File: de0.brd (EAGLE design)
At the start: 160 x 100 mm, 69 parts, among them IC1 PL2303SA__LF, J2 UX60SC-MB-5ST, U1 P0082, U2 RFM95W-915S2, U3 TPS76201DBVR, U4 TPS76201DBVR, U5 TPS76201DBVR

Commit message: Add files via upload
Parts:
- removed JP10: VDD, jumper:JP1
- removed JP8: VBP, jumper:JP1
- removed JP9: VBN, jumper:JP1
- added ADDRESS_0, ADDRESS_1, ADDRESS_10, ADDRESS_11, ADDRESS_12, ADDRESS_13, ADDRESS_14, ADDRESS_15, ADDRESS_2, ADDRESS_3, ADDRESS_4, ADDRESS_5, ADDRESS_6, ADDRESS_7, ADDRESS_8, ADDRESS_9, CLOCK, RD_DATA_0, RD_DATA_2, RD_DATA_3, RD_DATA_4, RD_DATA_5, RD_DATA_6, RD_DATA_7, RD_EN, U$4, U$40, U$48, U$49, U$50, U$51, U$52, U$53, USEC_TICK, WR_DATA_0, WR_DATA_1, WR_DATA_2, WR_DATA_3, WR_DATA_4, WR_DATA_5, WR_DATA_7, WR_EN: (no value), qfp160:POINT
- added C11, C13, C15, C20, C21, C22: 10uF, SparkFun-Capacitors:0603
- added C12, C14, C16, C17, C18, C19: 0.1uF, SparkFun-Capacitors:0603
- added J1: JUMPER_IN_50, jumper:04C
- added J3: REG_OUT_33, jumper:04C
- added JP13: REG_IN_07, jumper:JP1
- added JP14: REG_IN_12, jumper:JP1
- added JP15: REG_OUT_07, jumper:JP1
- added JP16: REG_OUT_12, jumper:JP1
- added JP17: VCCQ, jumper:JP1
- added JP18: VDDH, jumper:JP1
- added JP19: VDDLS, jumper:JP1
- added U$10: INTERRUPTS_0, qfp160:POINT
- added U$11: INTERRUPTS_1, qfp160:POINT
- added U$12: INTERRUPTS_2, qfp160:POINT
- added U$13: INTERRUPTS_3, qfp160:POINT
- added U$14, U$15: INTERRUPTS_5, qfp160:POINT
- added U$16: INTERRUPTS_6, qfp160:POINT
- added U$17: INTERRUPTS_7, qfp160:POINT
- JP3: value VDDLS -> VDD; device jumper:JP2Q -> jumper:JP1
- JP5: value LORA -> REG_IN_33; device jumper:JP6Q -> jumper:JP1
- JP6: value VCCQ -> VBP; device jumper:JP8Q -> jumper:JP1
- JP7: value VDDH -> VBN; device jumper:JP2Q -> jumper:JP1
- U$1: value (none) -> SOCKET
- moved JP7 188.2 mm to (73.1, -7.60)
- moved R7 187.2 mm to (-2.90, -15.8), turned to 90 degrees
- moved R6 186.7 mm to (0.10, -15.8), turned to 90 degrees
- moved R5 186.2 mm to (3.10, -15.8), turned to 90 degrees
- moved R4 185.7 mm to (6.10, -15.8), turned to 90 degrees
- moved R3 185.3 mm to (9.10, -15.8), turned to 90 degrees
- moved JP6 185.1 mm to (68.4, -7.40)
- moved R2 184.9 mm to (12.2, -15.8), turned to 90 degrees
- moved R1 184.4 mm to (15.2, -15.8), turned to 90 degrees
- moved JP12 183.6 mm to (74.0, -28.5)
- moved SV2 177.1 mm to (-53.5, -45.5)
- moved S5 174.4 mm to (30.9, -26.0), turned to 270 degrees
- moved D8 174.1 mm to (-5.90, -11.8), turned to 270 degrees
- moved D7 173.7 mm to (-2.90, -11.8), turned to 270 degrees
- moved D6 173.3 mm to (0.10, -11.8), turned to 268.9 degrees
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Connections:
- net GPIO-1_VCC_SYS renamed GPIO1_VCC_5V
- removed net GPIO-0_VCC3P3: U1.JP1_29
- removed net GPIO-0_VCC_SYS: U1.JP1_11
- removed net GPIO-1_VCC3P3: U1.JP2_29
- removed net N$12: JP2.7, U1.JP2_3
- removed net N$23: JP5.2, U2.2
- removed net N$25: JP5.6, U2.5
- removed net N$26: JP5.8, U2.6
- removed net N$28: JP5.12, U2.3
- removed net N$37: JP5.10, U2.14
- removed net VCCQ_0: JP6.2, U$1.49
- removed net VCCQ_1: JP6.4, U$1.62
- removed net VCCQ_2: JP6.6, U$1.83
- removed net VCCQ_3: JP6.8, U$1.93
- removed net VCCQ_4: JP6.10, U$1.105
- removed net VCCQ_5: JP6.12, U$1.114
- removed net VCCQ_6: JP6.14, U$1.135
- removed net VCCQ_7: JP6.16, U$1.145
- removed net VDDH_0: JP7.2, U$1.29
- removed net VDDH_1: JP7.4, U$1.99
- removed net VDDLS_0: JP3.2, U$1.33
- removed net VDDLS_1: JP3.4, U$1.103
- new net GPIO0_VCC_5V: J1.3, U1.JP1_11
- new net IN_07: C9.1, JP13.2, U3.1
- new net IN_12: C6.1, JP14.2, U4.1
- new net IN_33: C3.1, JP5.2, U5.1
- new net OUT_07: C10.1, JP15.1, R12.2, U3.5
- new net OUT_12: C7.1, JP16.1, R18.2, U4.5
- new net OUT_33: C4.1, J3.1, R19.2, U5.5
- new net VCCQ: C11.1, C12.1, JP17.2, U$1.105, U$1.114, U$1.135, U$1.145, U$1.49, U$1.62, U$1.83, U$1.93
- new net VDD5_USB: C2.+, D9.A, J1.1, J2.1
- new net VDDH: C13.1, C14.1, JP18.2, U$1.29, U$1.99
- new net VDDLS: C15.1, C16.1, JP19.2, U$1.103, U$1.33
- new net VO_FPGA_33: J3.3, U1.JP1_29, U1.JP2_29
- net ADDRESS_0: now also ADDRESS_0.1, U1.JP1_20; no longer U1.JP1_2
- net ADDRESS_1: now also ADDRESS_1.1, U1.JP1_22; no longer U1.JP1_4
- net ADDRESS_10: now also ADDRESS_10.1, U1.JP1_33; no longer U1.JP1_15
- net ADDRESS_11: now also ADDRESS_11.1, U1.JP1_35; no longer U1.JP1_16
- net ADDRESS_12: now also ADDRESS_12.1, U1.JP1_37; no longer U1.JP1_17
- net ADDRESS_13: now also ADDRESS_13.1, U1.JP1_39; no longer U1.JP1_18
- net ADDRESS_14: now also ADDRESS_14.1, U1.JP1_31; no longer U1.JP1_19
- net ADDRESS_15: now also ADDRESS_15.1, U1.JP1_27; no longer U1.JP1_21
- net ADDRESS_2: now also ADDRESS_2.1, U1.JP1_24; no longer U1.JP1_5
- net ADDRESS_3: now also ADDRESS_3.1, U1.JP1_26; no longer U1.JP2_31
- net ADDRESS_4: now also ADDRESS_4.1, U1.JP1_28; no longer U1.JP1_7
- net ADDRESS_5: now also ADDRESS_5.1, U1.JP1_32; no longer U1.JP1_8
- net ADDRESS_6: now also ADDRESS_6.1, U1.JP1_34; no longer U1.JP1_9
- net ADDRESS_7: now also ADDRESS_7.1, U1.JP1_36; no longer U1.JP1_10
- net ADDRESS_8: now also ADDRESS_8.1, U1.JP1_38; no longer U1.JP1_13
- net ADDRESS_9: now also ADDRESS_9.1, U1.JP1_40; no longer U1.JP1_14
- net CLOCK: now also CLOCK.1, U1.JP2_9; no longer U1.JP2_32
- net GND: now also C11.2, C12.2, C13.2, C14.2, C15.2, C16.2, C17.2, C18.2, C19.2, C20.2, C21.2, C22.2, JP7.1; no longer JP9.1
- net GPIO_OUT_0: now also U1.JP2_18; no longer U1.JP1_20
- net GPIO_OUT_1: now also U1.JP2_20; no longer U1.JP2_13
- net GPIO_OUT_2: now also U1.JP2_22; no longer U1.JP2_14
- net GPIO_OUT_3: now also U1.JP2_24; no longer U1.JP2_15
- net GPIO_OUT_4: now also U1.JP2_26; no longer U1.JP2_16
- net INTERRUPTS_0: now also U$10.1
- net INTERRUPTS_1: now also U$11.1
- net INTERRUPTS_2: now also U$12.1, U1.JP2_6; no longer U1.JP2_5
- net INTERRUPTS_3: now also U$13.1, U1.JP2_8; no longer U1.JP2_6
- net INTERRUPTS_4: now also U$14.1, U1.JP2_10; no longer U1.JP2_7
- net INTERRUPTS_5: now also U$15.1, U1.JP2_14; no longer U1.JP2_8
- net INTERRUPTS_6: now also U$16.1, U1.JP2_16; no longer U1.JP2_9
- net INTERRUPTS_7: now also U$17.1, U1.JP1_16; no longer U1.JP2_10
- net JTAG_TCK: now also U1.JP1_10; no longer U1.JP2_23
- net JTAG_TDI: now also U1.JP1_6; no longer U1.JP2_26
- net JTAG_TDO: now also U1.JP1_14; no longer U1.JP2_22
- net JTAG_TMS: now also U1.JP1_8; no longer U1.JP2_24
- net LORA_DIO0: now also U$53.1, U1.JP2_40, U2.14; no longer JP5.9, U1.JP2_35
- net LORA_MISO: now also U$48.1, U1.JP2_28, U2.2; no longer JP5.1, U1.JP2_36
- net LORA_MOSI: now also U$49.1, U1.JP2_32, U2.3; no longer JP5.11, U1.JP2_37
- net LORA_NSS: now also U$51.1, U1.JP2_36, U2.5; no longer JP5.5, U1.JP2_39
- net LORA_RESET: now also U$52.1, U1.JP2_38, U2.6; no longer JP5.7, U1.JP2_40
- net LORA_SCK: now also U$50.1, U1.JP2_34, U2.4; no longer JP5.3, U1.JP2_38
- net N$11: now also JP2.7; no longer JP2.5
- net N$24: now also JP2.5, U1.JP2_3; no longer JP5.4, U2.4
- net PIN_OUT_0: now also U1.JP2_25; no longer U1.JP1_6
- net PIN_OUT_2: now also U1.JP2_31; no longer U1.JP2_28
- net RD_DATA_0: now also RD_DATA_0.1, U1.JP2_23; no longer U1.JP1_32
- net RD_DATA_1: now also U$4.1, U1.JP2_21; no longer U1.JP1_33
- net RD_DATA_2: now also RD_DATA_2.1, U1.JP2_19; no longer U1.JP1_34
- net RD_DATA_3: now also RD_DATA_3.1, U1.JP2_17; no longer U1.JP1_35
- net RD_DATA_4: now also RD_DATA_4.1, U1.JP2_15; no longer U1.JP1_36
- net RD_DATA_5: now also RD_DATA_5.1, U1.JP2_13; no longer U1.JP1_37
- net RD_DATA_6: now also RD_DATA_6.1, U1.JP2_7; no longer U1.JP1_38
- net RD_DATA_7: now also RD_DATA_7.1, U1.JP2_5; no longer U1.JP1_39
- net RD_EN: now also RD_EN.1, U1.JP1_5; no longer U1.JP2_25
- net SPI_CS: now also U1.JP2_33; no longer U1.JP2_17
- net SPI_MISO: now also U1.JP2_35; no longer U1.JP2_19
- net SPI_MOSI: now also U1.JP2_37; no longer U1.JP2_20
- net SPI_SCK: now also U1.JP2_39; no longer U1.JP2_21
- net UART_RX: now also U1.JP1_4; no longer U1.JP2_33
- net UART_TX: now also U1.JP1_2; no longer U1.JP2_34
- net USEC_TICK: now also U1.JP1_18, USEC_TICK.1; no longer U1.JP2_18
- net VBN: now also C17.1, C21.1, JP7.2; no longer JP9.2
- net VBP: now also C18.1, C20.1, JP6.2; no longer JP8.2
- net VDD: now also C19.1, C22.1, JP3.2; no longer JP10.2
- net VDD5: now also J1.2, JP13.1, JP14.1, JP5.1; no longer C2.+, C3.1, C6.1, C9.1, D9.A, J2.1, U3.1, U4.1, U5.1
- net VO_07: now also JP15.2, JP19.1; no longer C10.1, JP3.1, JP3.3, R12.2, U3.5
- net VO_12: now also JP16.2, JP18.1, JP3.1, JP6.1; no longer C7.1, JP10.1, JP7.1, JP7.3, JP8.1, R18.2, U4.5
- net VO_33: now also J3.2, JP17.1; no longer C4.1, JP6.1, JP6.11, JP6.13, JP6.15, JP6.3, JP6.5, JP6.7, JP6.9, R19.2, U5.5
- net WR_DATA_0: now also U1.JP1_23, WR_DATA_0.1; no longer U1.JP1_22
- net WR_DATA_1: now also U1.JP1_21, WR_DATA_1.1; no longer U1.JP1_23
- net WR_DATA_2: now also U1.JP1_19, WR_DATA_2.1; no longer U1.JP1_24
- net WR_DATA_3: now also U1.JP1_17, WR_DATA_3.1; no longer U1.JP1_25
- net WR_DATA_4: now also U1.JP1_15, WR_DATA_4.1; no longer U1.JP1_26
- net WR_DATA_5: now also U1.JP1_13, WR_DATA_5.1; no longer U1.JP1_27
- net WR_DATA_6: now also U$40.1, U1.JP1_9; no longer U1.JP1_28
- net WR_DATA_7: now also U1.JP1_7, WR_DATA_7.1; no longer U1.JP1_31
- net WR_EN: now also U1.JP1_25, WR_EN.1; no longer U1.JP1_40
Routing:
- net INTERRUPTS_6: track 0.00 -> 147.6 mm
- net INTERRUPTS_5: track 0.00 -> 144.1 mm
- net INTERRUPTS_4: track 0.00 -> 136.4 mm
- net INTERRUPTS_3: track 0.00 -> 131.5 mm
- net INTERRUPTS_2: track 0.00 -> 126.5 mm
- net INTERRUPTS_1: track 0.00 -> 122.1 mm
- net INTERRUPTS_0: track 0.00 -> 115.2 mm
- net USEC_TICK: track 0.00 -> 108.4 mm
- net INTERRUPTS_7: track 0.00 -> 108.4 mm
- net ADDRESS_0: track 0.00 -> 105.1 mm
- net ADDRESS_1: track 0.00 -> 102.0 mm
- net ADDRESS_2: track 0.00 -> 100.4 mm
- net GND: track 0.00 -> 99.2 mm
- net RD_DATA_4: track 0.00 -> 95.2 mm
- net WR_DATA_7: track 0.00 -> 94.7 mm, vias 0 -> 1
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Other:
- board size 160 x 100 mm -> 148.8 x 90.3 mm

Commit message: Connect source for switches
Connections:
- net VO_33: now also S1.1, S2.1, S3.1, S4.1, S5.1, S6.1
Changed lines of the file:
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@@
 <contactref element="J3" pad="2"/>
 <contactref element="JP17" pad="1"/>
+<contactref element="S5" pad="1"/>
+<contactref element="S6" pad="1"/>
+<contactref element="S4" pad="1"/>
+<contactref element="S3" pad="1"/>
+<contactref element="S2" pad="1"/>
+<contactref element="S1" pad="1"/>
+<wire x1="-3.2" y1="-21.89" x2="-21.45" y2="-29.76" width="0" layer="19" extent="1-1"/>
+<wire x1="3.7" y1="-21.89" x2="-3.2" y2="-21.89" width="0" layer="19" extent="1-1"/>
+<wire x1="10.4" y1="-21.79" x2="3.7" y2="-21.89" width="0" layer="19" extent="1-1"/>
+<wire x1="16.9" y1="-21.79" x2="10.4" y2="-21.79" width="0" layer="19" extent="1-1"/>
+<wire x1="30.85" y1="-22.19" x2="16.9" y2="-21.79" width="0" layer="19" extent="1-1"/>
+<wire x1="38.3" y1="-21.99" x2="30.85" y2="-22.19" width="0" layer="19" extent="1-1"/>
+<wire x1="48.1" y1="-8.57" x2="38.3" y2="-21.99" width="0" layer="19" extent="1-1"/>
+<wire x1="-30.3" y1="3.12" x2="-21.45" y2="-29.76" width="0" layer="19" extent="1-1"/>
+<wire x1="-32.72" y1="3.53" x2="-30.3" y2="3.12" width="0" layer="19" extent="1-1"/>
+<wire x1="-19.695" y1="18.6" x2="-30.3" y2="3.12" width="0" layer="19" extent="1-1"/>
+<wire x1="-46.435" y1="16.768" x2="-32.72" y2="3.53" width="0" layer="19" extent="1-1"/>
+<wire x1="-48.975" y1="22.192" x2="-46.435" y2="16.768" width="0" layer="19" extent="1-1"/>
 </signal>
 <signal name="VO_07">

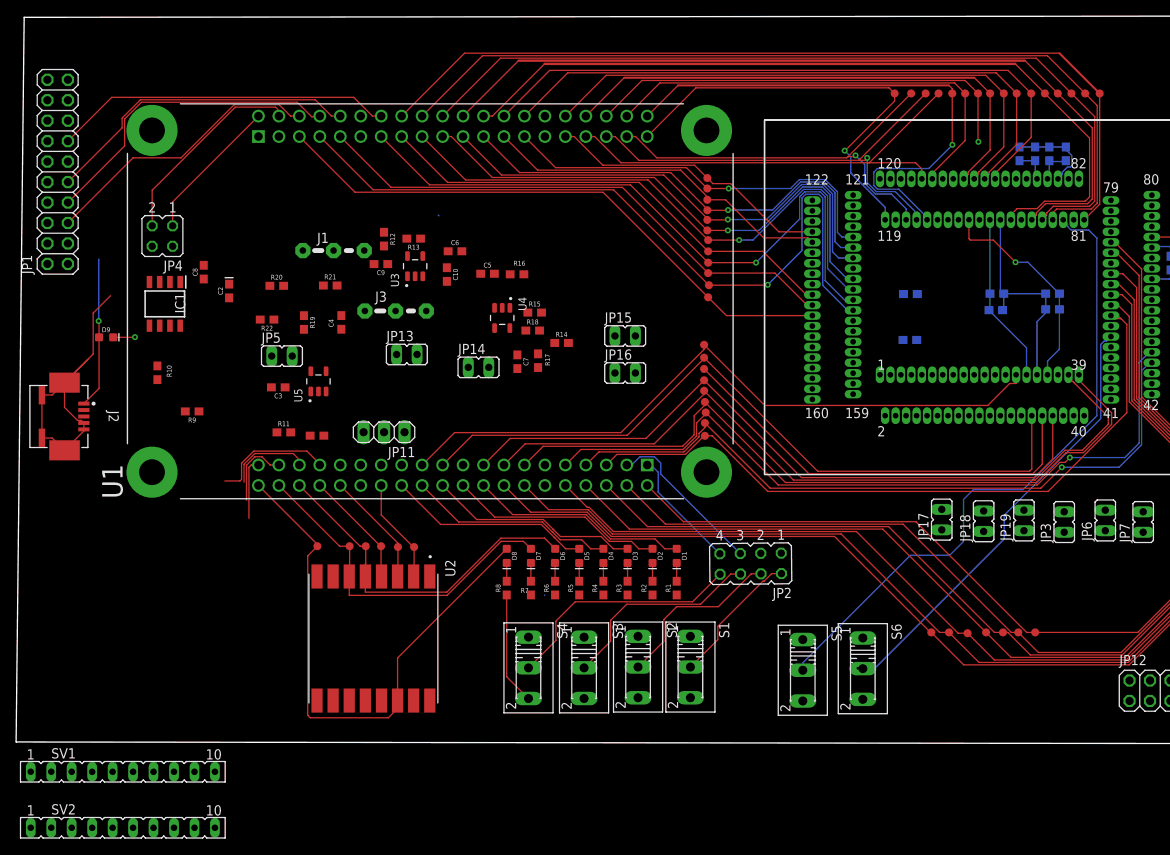
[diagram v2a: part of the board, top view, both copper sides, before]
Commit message: Organize regulator circuits
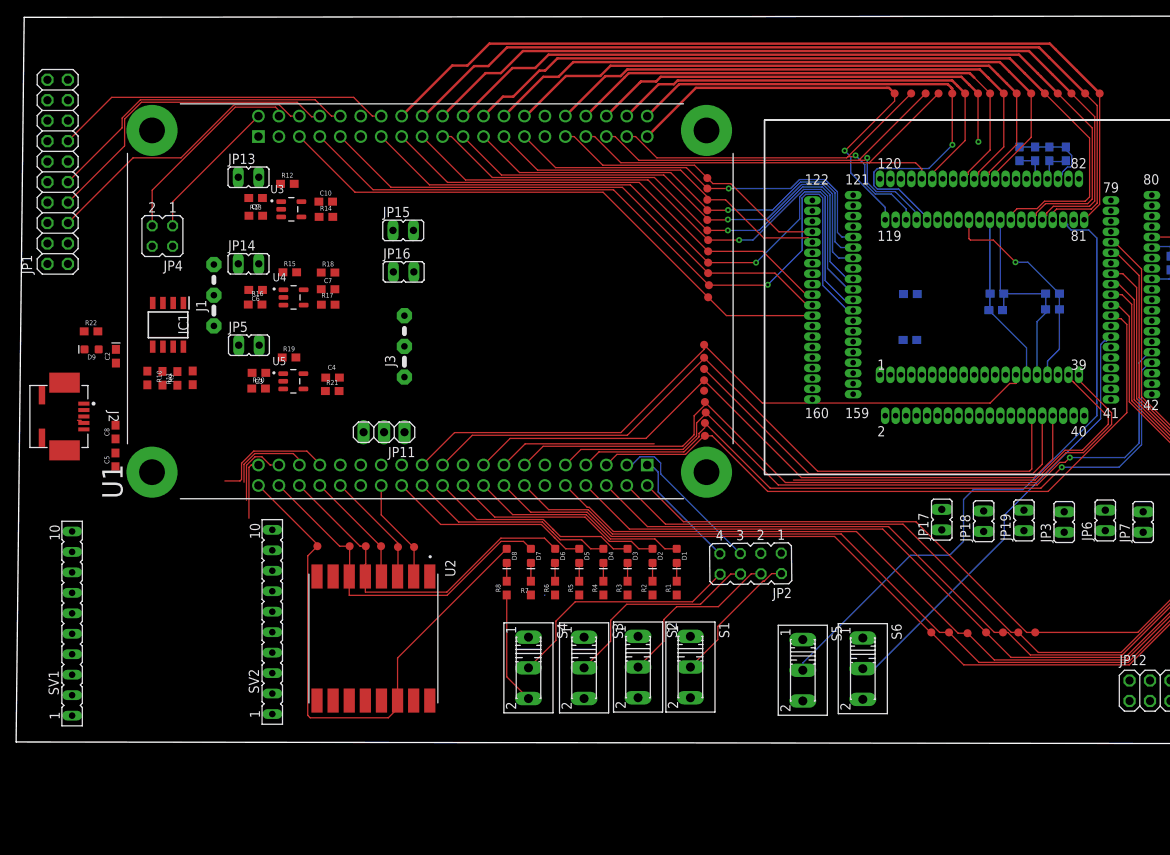
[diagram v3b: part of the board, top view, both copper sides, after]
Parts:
- moved C5 51.6 mm to (-54.5, 0.12), turned to 90 degrees
- moved R14 33.2 mm to (-28.3, 30.3)
- moved R16 32.7 mm to (-37.1, 19.4)
- moved SV2 31.6 mm to (-35.0, -20.0), turned to 90 degrees
- moved JP14 31.3 mm to (-38.0, 24.4)
- moved R15 30.8 mm to (-32.8, 23.4)
- moved JP15 30.5 mm to (-18.8, 28.6)
- moved JP16 30.2 mm to (-18.7, 23.4)
- moved JP13 29.5 mm to (-38.0, 35.2)
- moved R17 27.0 mm to (-28.1, 19.4), turned to 0 degrees
- moved R18 26.4 mm to (-28.1, 23.4)
- moved U4 26.0 mm to (-32.4, 20.3), turned to 0 degrees
- moved C6 25.2 mm to (-37.1, 21.2), turned to 180 degrees
- moved C7 25.2 mm to (-28.1, 21.3), turned to 0 degrees
- moved C8 22.7 mm to (-54.5, 3.57)
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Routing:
- net GND: track 99.2 -> 59.5 mm
- net RD_DATA_4: track 95.2 -> 69.9 mm
- net VDD5_USB: track 18.8 -> 0.00 mm, vias 1 -> 0
- net INTERRUPTS_7: track 108.4 -> 116.5 mm
- net ADDRESS_6: track 64.9 -> 72.1 mm
- net ADDRESS_0: track 105.1 -> 108.2 mm
- net ADDRESS_1: track 102.0 -> 104.8 mm
- net N$36: track 2.74 -> 0.00 mm, vias 1 -> 0
- net LOCKED: track 56.2 -> 53.5 mm, vias 1 -> 0
- net ADDRESS_3: track 81.5 -> 84.0 mm
- net ADDRESS_2: track 100.4 -> 102.6 mm
- net USEC_TICK: track 108.4 -> 109.9 mm
- net ADDRESS_7: track 54.7 -> 55.8 mm
- net ADDRESS_4: track 76.6 -> 77.7 mm
- net ADDRESS_5: track 69.6 -> 70.5 mm
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
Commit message: Update layout
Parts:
- moved JP7 76.5 mm to (5.80, 28.7), turned to 270 degrees
- moved JP6 70.7 mm to (5.90, 25.8), turned to 270 degrees
- moved JP3 64.9 mm to (5.90, 22.8), turned to 270 degrees
- moved JP19 59.0 mm to (5.90, 19.6), turned to 270 degrees
- moved JP18 53.1 mm to (5.90, 16.4), turned to 270 degrees
- moved JP17 47.0 mm to (5.85, 13.3), turned to 270 degrees
- moved U$10 16.2 mm to (47.8, -10.3)
- moved U$11 16.0 mm to (45.9, -10.3)
- moved U$12 16.0 mm to (44.1, -10.3)
- moved U$13 15.7 mm to (42.3, -10.3)
- moved U$14 15.5 mm to (40.5, -10.3)
- moved U$15 15.1 mm to (38.6, -10.3)
- moved U$16 14.8 mm to (36.9, -10.3)
- moved C9 3.93 mm to (-34.2, 29.9), turned to 0 degrees
- moved U3 3.22 mm to (-29.4, 30.9)
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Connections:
- net GND: now also U$1.35, U$1.67
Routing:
- net GND: track 59.5 -> 296.2 mm, vias 0 -> 8
- net VO_33: track 0.00 -> 168.1 mm, vias 0 -> 1
- net VCCQ: track 0.00 -> 140.5 mm, vias 0 -> 4
- net N$10: track 0.00 -> 139.1 mm, vias 0 -> 2
- net N$9: track 0.00 -> 137.9 mm, vias 0 -> 3
- net VDD: track 5.82 -> 87.9 mm, vias 0 -> 2
- net VBP: track 4.43 -> 67.2 mm, vias 0 -> 4
- net VDDH: track 21.2 -> 80.9 mm, vias 0 -> 2
- net VDDLS: track 27.1 -> 86.6 mm, vias 1 -> 3
- net VBN: track 4.29 -> 61.0 mm
- net VO_FPGA_33: track 0.00 -> 53.5 mm
- net VDD5: track 0.00 -> 34.0 mm, vias 0 -> 1
- net SPI_SCK: track 7.63 -> 41.3 mm
- net SPI_MOSI: track 9.23 -> 42.9 mm
- net VO_12: track 0.00 -> 33.2 mm, vias 0 -> 1
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- added copper zone on layer 1, net GND
- added copper zone on layer 16, net V0_12
- added copper zone on layer 16, net VBN
- added copper zone on layer 16, net VBP
- added copper zone on layer 1, net VCCQ
- added copper zone on layer 16, net VCCQ
- added copper zone on layer 1, net VDD
- added copper zone on layer 16, net VDD
- added copper zone on layer 1, net VDDH
- added copper zone on layer 16, net VDDH
- added copper zone on layer 1, net VDDLS
- added copper zone on layer 16, net VDDLS
- added copper zone on layer 1, net VO_07
- added copper zone on layer 1, net VO_12
- added copper zone on layer 16, net VO_33
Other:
- board size 148.8 x 90.3 mm -> 150.7 x 90.7 mm

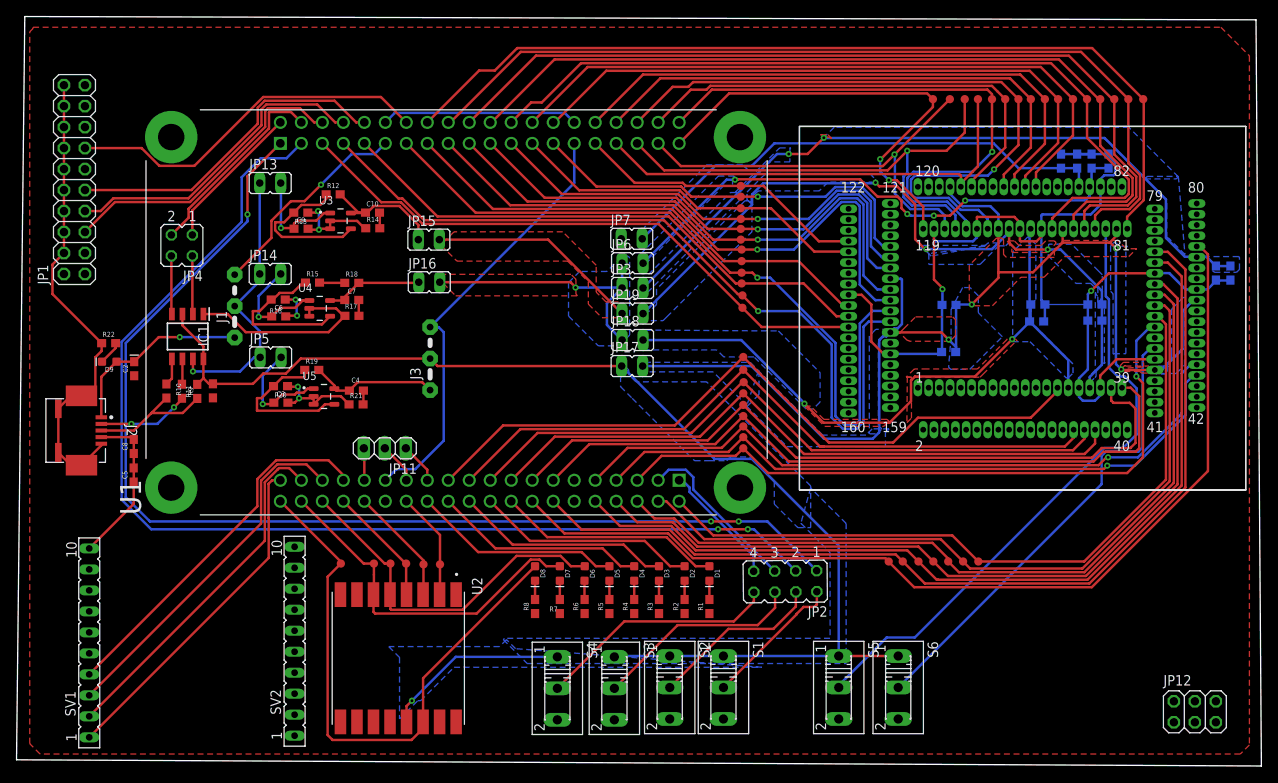
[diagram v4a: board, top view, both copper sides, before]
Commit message: Create plain for power wires
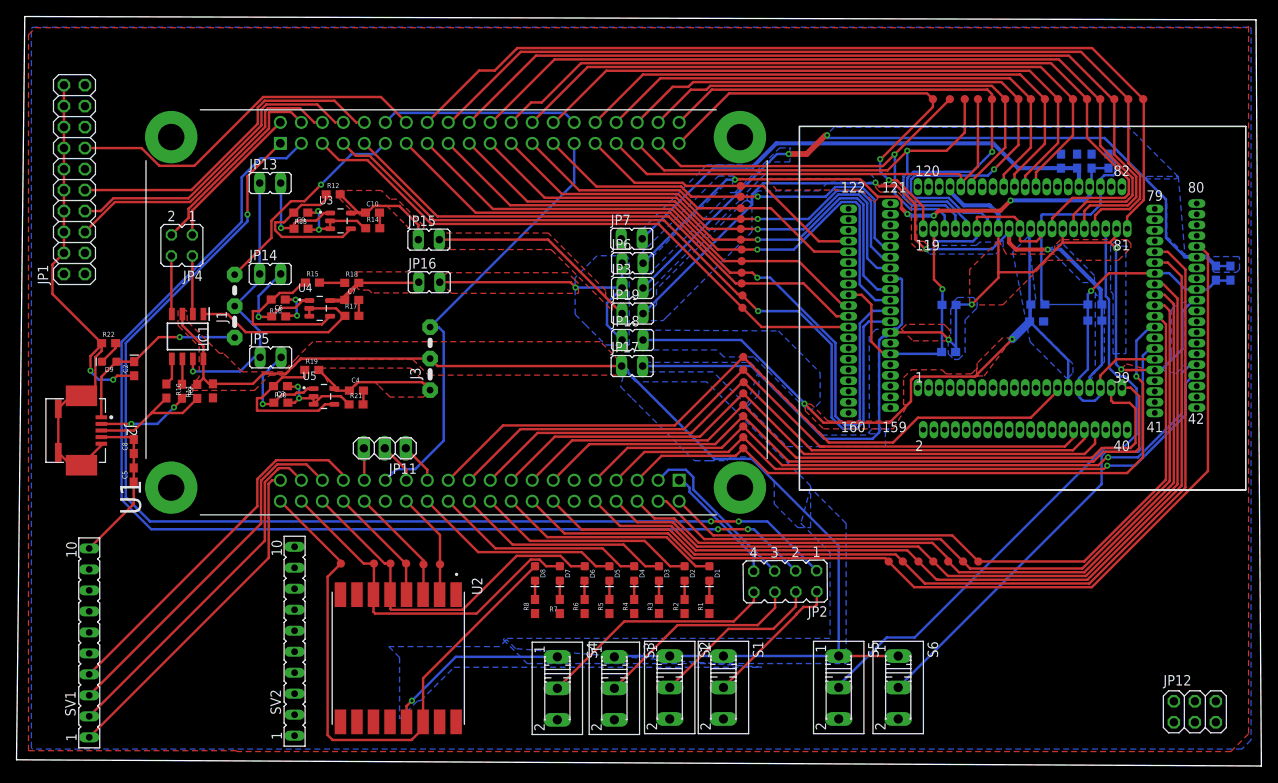
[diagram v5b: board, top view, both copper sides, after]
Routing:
- net GND: track 296.2 -> 295.7 mm, vias 8 -> 10
- added copper zone on layer 16, net GND
- added copper zone on layer 1, net OUT_07
- added copper zone on layer 1, net OUT_12
- added copper zone on layer 1, net OUT_33
- added copper zone on layer 1, net VBP
- added copper zone on layer 16, net VO_12
- added copper zone on layer 1, net VO_33
- removed copper zone on layer 16, net V0_12
- removed copper zone on layer 1, net VDD
